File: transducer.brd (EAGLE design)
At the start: 33 x 33 mm, 12 parts, among them U1 ADS1014IDGST

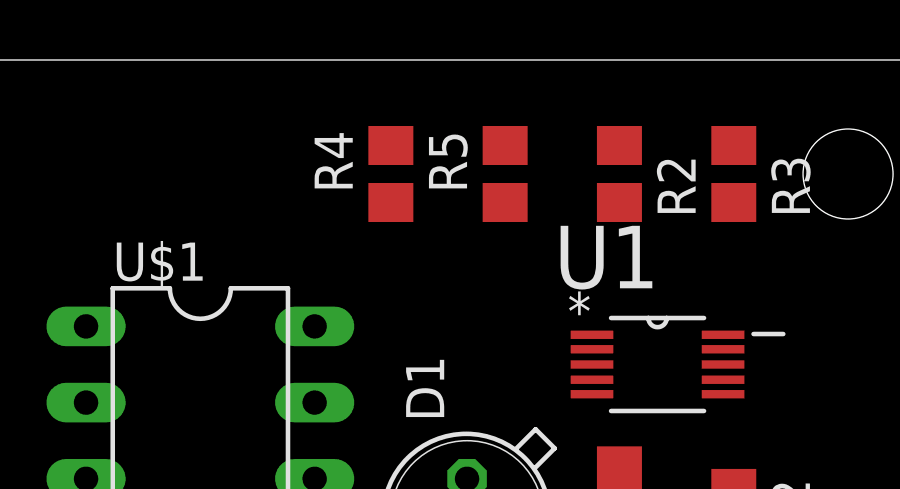
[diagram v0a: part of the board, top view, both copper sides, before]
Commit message: updated pullups
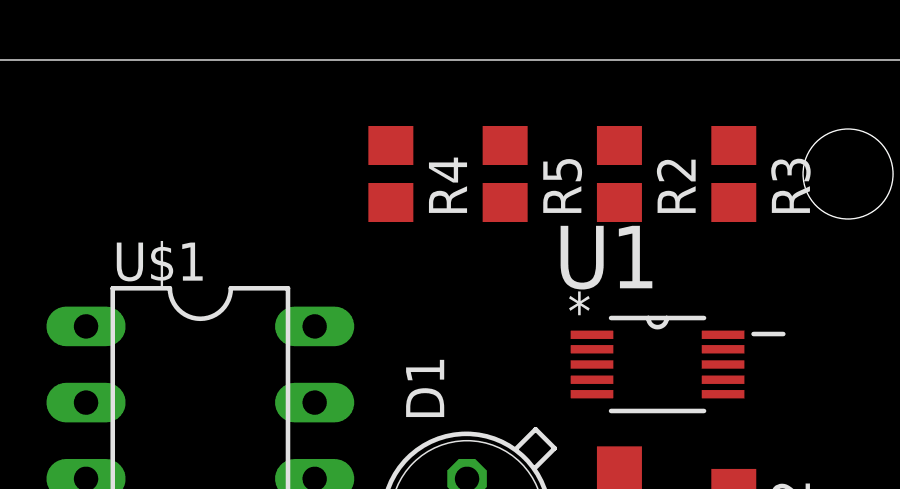
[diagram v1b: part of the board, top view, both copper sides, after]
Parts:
- turned R4 to 270 degrees
- turned R5 to 270 degrees
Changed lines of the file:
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@@
 <attribute name="SPICEPREFIX" value="R" x="25.4" y="76.2" size="1.778" layer="27" rot="R270" display="off"/>
 </element>
-<element name="R4" library="rcl" library_urn="urn:adsk.eagle:library:334" package="R0805" package3d_urn="urn:adsk.eagle:package:23553/2" value="0" x="13.97" y="76.2" rot="R90">
-<attribute name="SPICEPREFIX" value="R" x="13.97" y="76.2" size="1.778" layer="27" rot="R90" display="off"/>
+<element name="R4" library="rcl" library_urn="urn:adsk.eagle:library:334" package="R0805" package3d_urn="urn:adsk.eagle:package:23553/2" value="0" x="13.97" y="76.2" rot="R270">
+<attribute name="SPICEPREFIX" value="R" x="13.97" y="76.2" size="1.778" layer="27" rot="R270" display="off"/>
 </element>
-<element name="R5" library="rcl" library_urn="urn:adsk.eagle:library:334" package="R0805" package3d_urn="urn:adsk.eagle:package:23553/2" value="0" x="17.78" y="76.2" rot="R90">
-<attribute name="SPICEPREFIX" value="R" x="17.78" y="76.2" size="1.778" layer="27" rot="R90" display="off"/>
+<element name="R5" library="rcl" library_urn="urn:adsk.eagle:library:334" package="R0805" package3d_urn="urn:adsk.eagle:package:23553/2" value="0" x="17.78" y="76.2" rot="R270">
+<attribute name="SPICEPREFIX" value="R" x="17.78" y="76.2" size="1.778" layer="27" rot="R270" display="off"/>
 </element>
 <element name="D1" library="diode" library_urn="urn:adsk.eagle:library:210" package="TO18D" package3d_urn="urn:adsk.eagle:package:43443/1" value="" x="16.51" y="64.77" rot="R90"/>
@@
 <contactref element="U1" pad="9"/>
 <contactref element="R4" pad="2"/>
-<wire x1="13.97" y1="77.15" x2="25.0444" y2="70.358" width="0" layer="19" extent="1-1"/>
+<wire x1="13.97" y1="75.25" x2="25.0444" y2="70.358" width="0" layer="19" extent="1-1"/>
 <wire x1="15.24" y1="58.42" x2="25.0444" y2="70.358" width="0" layer="19" extent="1-1"/>
 </signal>
@@
 <contactref element="U1" pad="10"/>
 <contactref element="R5" pad="2"/>
-<wire x1="25.0444" y1="70.8406" x2="17.78" y2="77.15" width="0" layer="19" extent="1-1"/>
+<wire x1="25.0444" y1="70.8406" x2="17.78" y2="75.25" width="0" layer="19" extent="1-1"/>
 <wire x1="17.78" y1="58.42" x2="25.0444" y2="70.8406" width="0" layer="19" extent="1-1"/>
 </signal>
@@
 <contactref element="R2" pad="1"/>
 <wire x1="21.59" y1="77.15" x2="25.4" y2="77.15" width="0" layer="19" extent="1-1"/>
-<wire x1="17.78" y1="75.25" x2="21.59" y2="77.15" width="0" layer="19" extent="1-1"/>
-<wire x1="13.97" y1="75.25" x2="17.78" y2="75.25" width="0" layer="19" extent="1-1"/>
-<wire x1="20.6756" y1="70.8406" x2="17.78" y2="75.25" width="0" layer="19" extent="1-1"/>
+<wire x1="17.78" y1="77.15" x2="21.59" y2="77.15" width="0" layer="19" extent="1-1"/>
+<wire x1="13.97" y1="77.15" x2="17.78" y2="77.15" width="0" layer="19" extent="1-1"/>
+<wire x1="20.6756" y1="70.8406" x2="17.78" y2="77.15" width="0" layer="19" extent="1-1"/>
 </signal>
 <signal name="N$8">

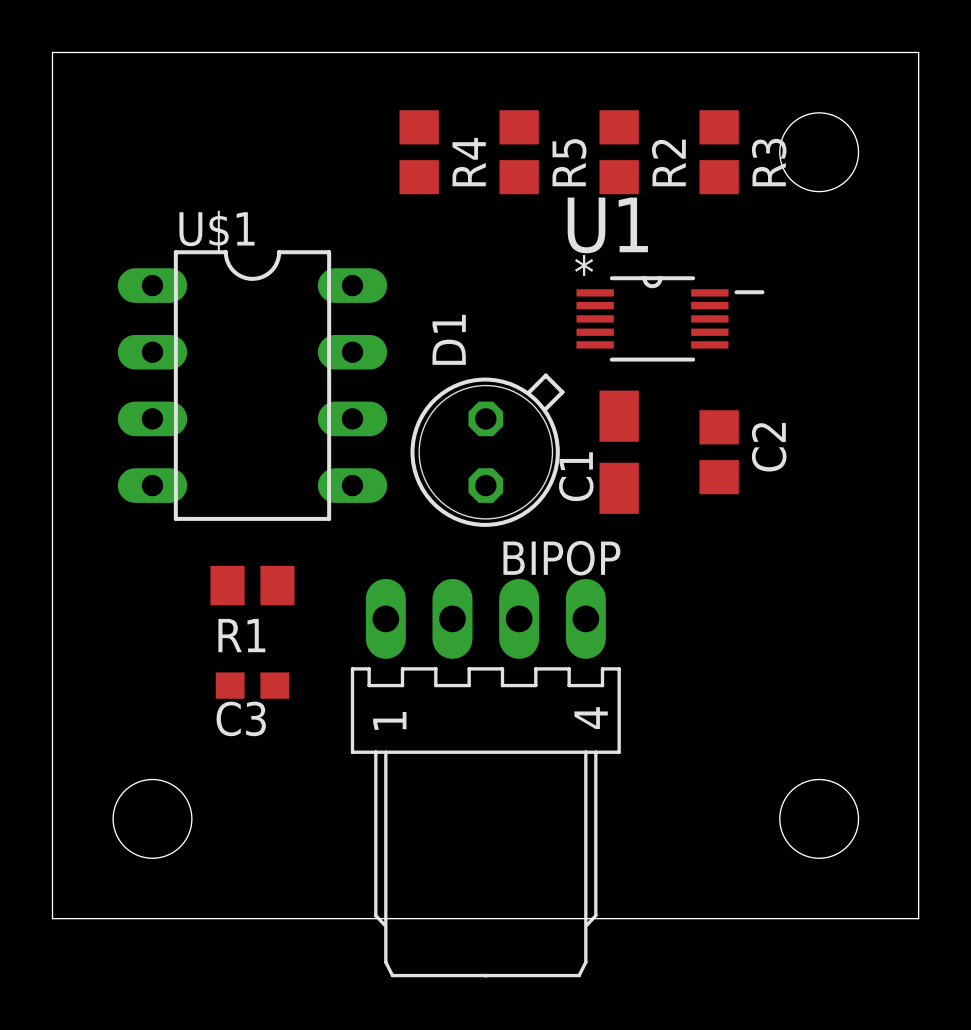
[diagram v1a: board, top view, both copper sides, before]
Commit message: Transducer board routed.
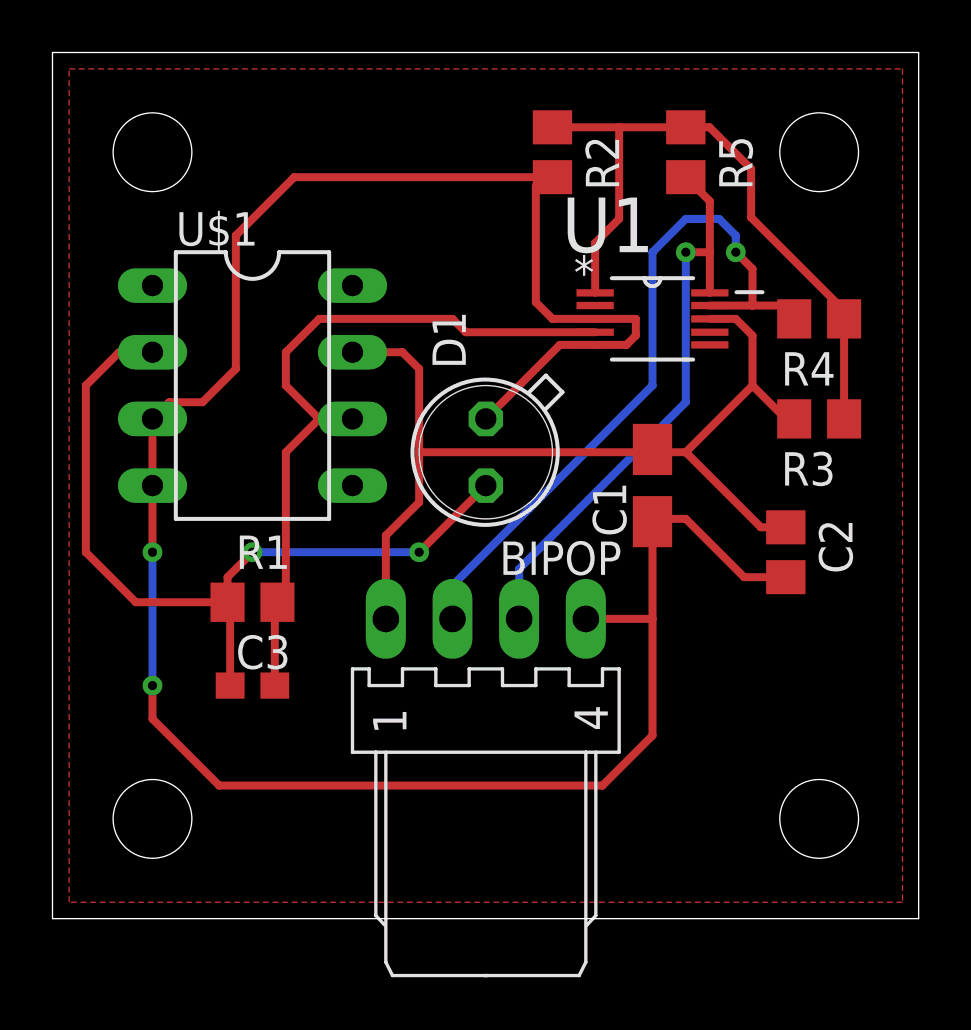
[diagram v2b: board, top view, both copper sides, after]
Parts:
- moved R4 16.5 mm to (29.2, 69.8), turned to 180 degrees
- moved R3 10.9 mm to (29.2, 66.0), turned to 180 degrees
- moved R5 6.35 mm to (24.1, 76.2)
- moved C2 4.58 mm to (27.9, 61.0)
- moved R2 2.54 mm to (19.1, 76.2)
- moved C1 1.80 mm to (22.9, 63.5)
- moved R1 0.63 mm to (7.62, 59.1), turned to 0 degrees
- turned C3 to 0 degrees
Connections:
- net N$3 renamed ADR
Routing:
- net GND: track 0.00 -> 87.3 mm, vias 0 -> 2
- net 3.3V: track 0.00 -> 37.6 mm
- net N$5: track 0.00 -> 31.0 mm, vias 0 -> 2
- net U_OUT: track 0.00 -> 28.3 mm
- net SDA: track 0.00 -> 27.4 mm, vias 0 -> 1
- net ADR: track 0.00 -> 25.9 mm
- net SCL: track 0.00 -> 22.3 mm, vias 0 -> 1
- added copper zone on layer 1, net GND
